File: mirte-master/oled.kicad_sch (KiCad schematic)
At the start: 1 part, among them J8 oled_conn

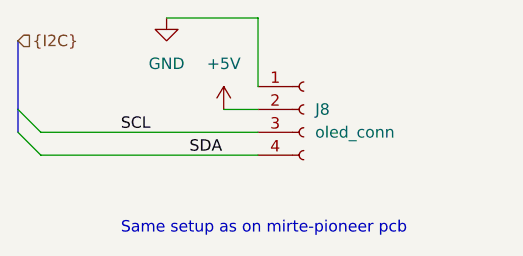
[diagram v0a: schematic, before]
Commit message: mirte-master schematic cleanup and readabilityimprovements
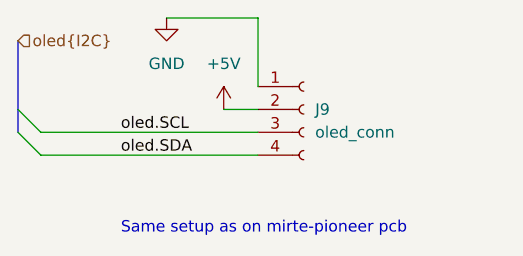
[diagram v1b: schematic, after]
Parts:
- renumbered J8 to J9
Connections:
- net SCL renamed oled.SCL
- net SDA renamed oled.SDA
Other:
- title: (none) -> ${PROJECTNAME}
